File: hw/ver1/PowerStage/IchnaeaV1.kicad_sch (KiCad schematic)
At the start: 11 parts, among them J2 Conn_02x12_Odd_Even, J3 Screw_Terminal_01x09, J4 Screw_Terminal_01x09, J5 Screw_Terminal_01x09, J6 Screw_Terminal_01x09, J8 FanConnector

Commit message: More power plane work. Double mosfets.
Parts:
- added HS1: Heatsink, symbol Mechanical:Heatsink
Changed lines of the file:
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@@
+	)
+	(symbol
+		(lib_id "Mechanical:Heatsink")
+		(at 157.48 44.45 0)
+		(unit 1)
+		(exclude_from_sim no)
+		(in_bom yes)
+		(on_board yes)
+		(dnp no)
+		(fields_autoplaced yes)
+		(property "Reference" "HS1"
+			(at 161.29 41.2749 0)
+			(effects
+				(font
+					(size 1.27 1.27)
+				)
+				(justify left)
+			)
+		)
+		(property "Value" "Heatsink"
+			(at 161.29 43.8149 0)
+			(effects
+				(font
+					(size 1.27 1.27)
+				)
+				(justify left)
+			)
+		)
+		(property "Footprint" ""
+			(at 157.7848 44.45 0)
+			(effects
+				(font
+					(size 1.27 1.27)
+				)
+				(hide yes)
+			)
+		)
+		(property "Datasheet" "~"
+			(at 157.7848 44.45 0)
+			(effects
+				(font
+					(size 1.27 1.27)
+				)
+				(hide yes)
+			)
+		)
+		(property "Description" "Heatsink"
+			(at 157.48 44.45 0)
+			(effects
+				(font
+					(size 1.27 1.27)
+				)
+				(hide yes)
+			)
+		)
+		(instances
+			(project "IchnaeaV1"
+				(path "/1a8ad36a-4b76-4949-97c2-661f12a0b1d9"
+					(reference "HS1")
+					(unit 1)
+				)
+			)
+		)
 	)
 	(symbol

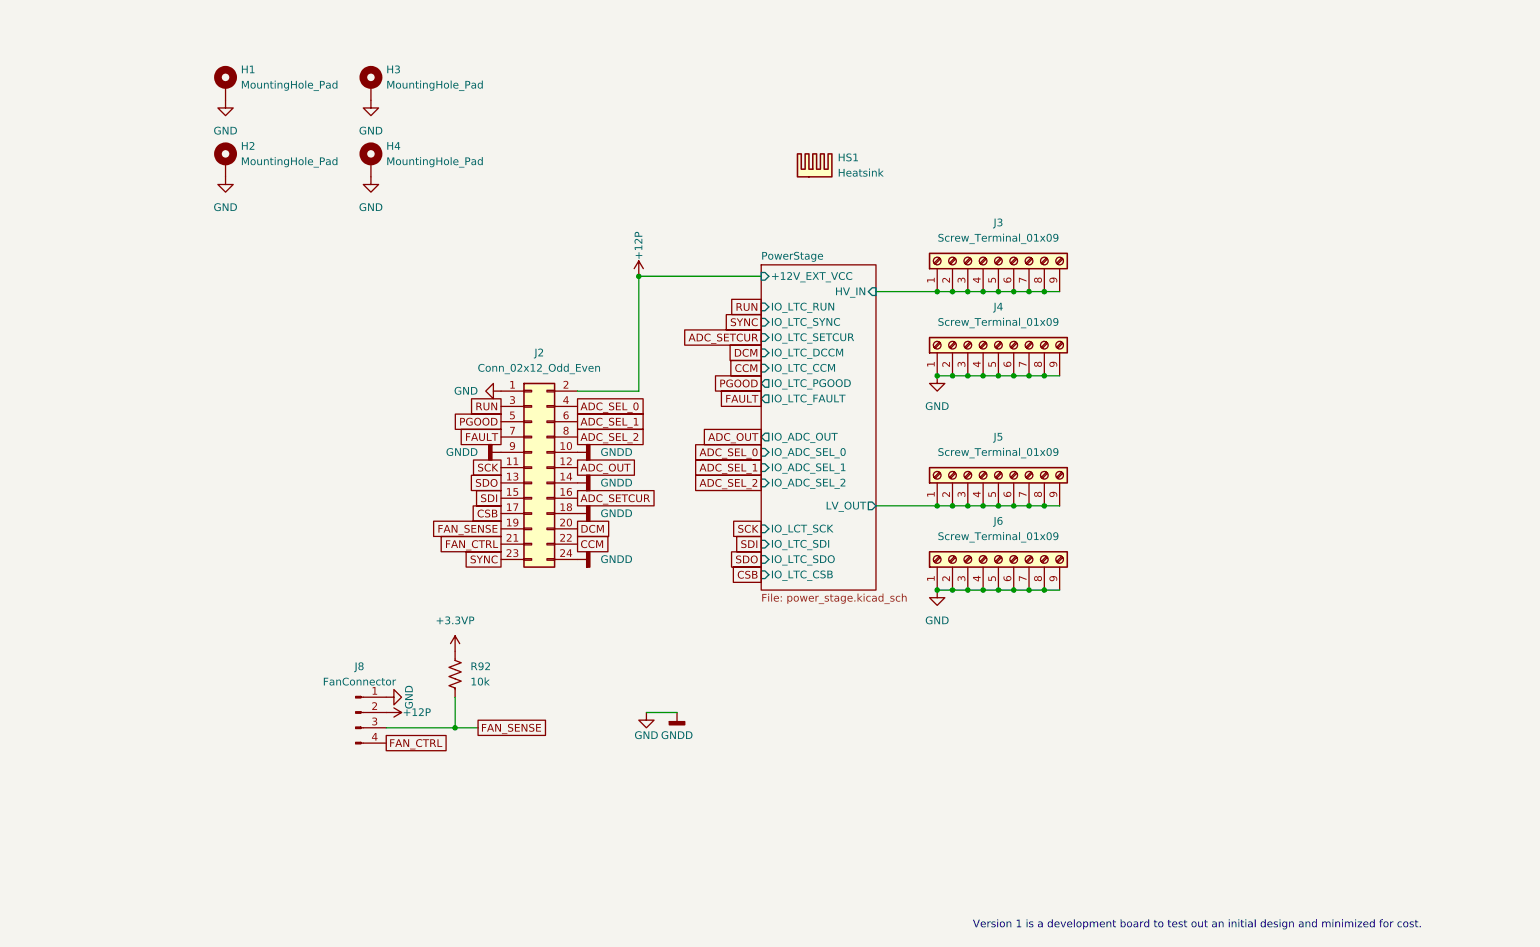
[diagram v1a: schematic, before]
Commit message: Improve power layout. Finish most of the initial routing for the LTC7871
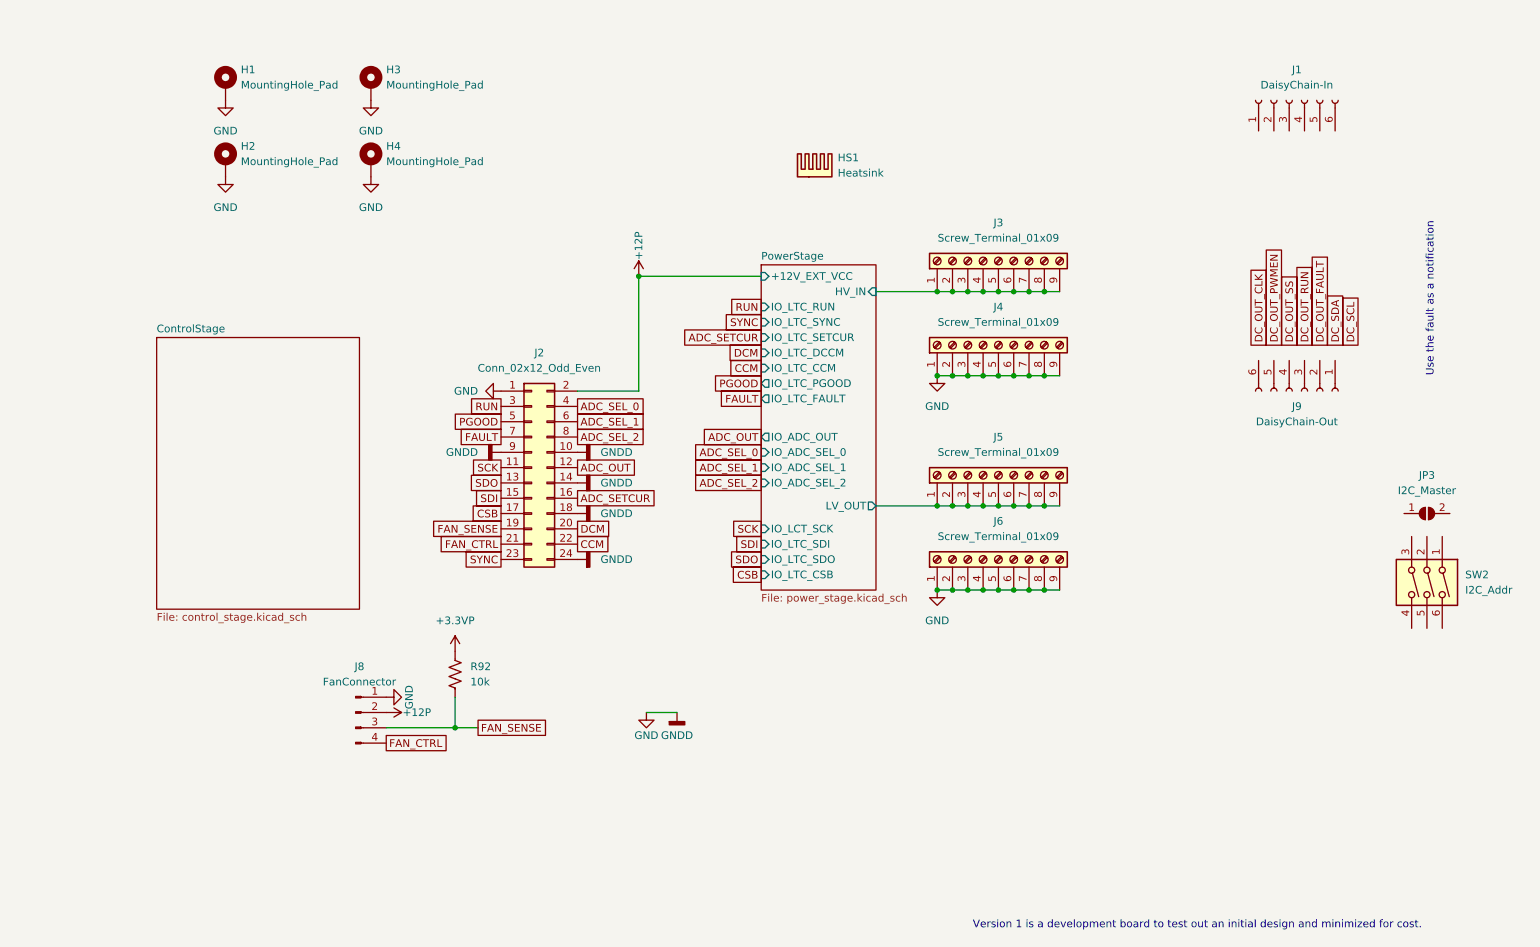
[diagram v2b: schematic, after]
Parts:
- added J1: DaisyChain-In, symbol Connector:Conn_01x06_Socket
- added J9: DaisyChain-Out, symbol Connector:Conn_01x06_Socket
- added JP3: I2C_Master, symbol Jumper:SolderJumper_2_Open
- added SW2: I2C_Addr, Button_Switch_SMD:SW_DIP_SPSTx03_Slide_6.7x9.18mm_W6.73mm_P2.54mm_LowProfile_JPin, symbol Switch:SW_DIP_x03
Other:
- added sheet ControlStage (control_stage.kicad_sch)
- note added: "Use the fault as a notification"

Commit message: Sync morning work to laptop
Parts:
- removed J2: Conn_02x12_Odd_Even, Connector_PinSocket_2.54mm:PinSocket_2x12_P2.54mm_Vertical, symbol Connector_Generic:Conn_02x12_Odd_Even
- removed J8: FanConnector, Connector_Molex:Molex_KK-254_AE-6410-04A_1x04_P2.54mm_Vertical, symbol Connector:Conn_01x04_Pin
- removed JP3: I2C_Master, symbol Jumper:SolderJumper_2_Open
- removed R92: 10k, Resistor_SMD:R_0603_1608Metric, symbol Device:R_US
- removed SW2: I2C_Addr, Button_Switch_SMD:SW_DIP_SPSTx03_Slide_6.7x9.18mm_W6.73mm_P2.54mm_LowProfile_JPin, symbol Switch:SW_DIP_x03
- J1, J9: footprint (none) -> Connector_PinHeader_1.27mm:PinHeader_2x05_P1.27mm_Vertical_SMD; symbol Connector:Conn_01x06_Socket -> Connector:Conn_01x10_Pin
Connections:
- net GND: now also J1.2 (Pin_2), J1.9 (Pin_9), J9.1 (Pin_1), J9.10 (Pin_10)
- net PowerStage/DC_OUT_SDA: now reaches J9.2 (Pin_2)
- net PowerStage/DC_OUT_SS: now reaches J9.3 (Pin_3)
- net PowerStage/DC_OUT_SCL: now reaches J9.4 (Pin_4)
- net PowerStage/DC_OUT_PWMEN: now reaches J9.5 (Pin_5)
- net PowerStage/DC_IN_SYNC: now reaches J1.1 (Pin_1)
- net PowerStage/DC_IN_RUN: now reaches J1.3 (Pin_3)
- net PowerStage/DC_IN_EN: now reaches J1.4 (Pin_4)
- net PowerStage/DC_IN_PWMEN: now reaches J1.5 (Pin_5)
- new net PowerStage/DC_IN_SCL: J1.8 (Pin_8)
- new net PowerStage/DC_IN_SDA: J1.10 (Pin_10)
- new net PowerStage/DC_IN_SS: J1.7 (Pin_7)
- new net PowerStage/DC_OUT_CLK: J9.9 (Pin_9)
- new net PowerStage/DC_OUT_EN: J9.8 (Pin_8)
- new net PowerStage/DC_OUT_RUN: J9.7 (Pin_7)
- no-connect marks 0 -> 2
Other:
- sheet PowerStage ports: added +3V3, +5V, DC_IN_EN, DC_IN_PWMEN, DC_IN_RUN, DC_IN_SCL, DC_IN_SDA, DC_IN_SS, DC_IN_SYNC, DC_OUT_CLK, DC_OUT_EN, DC_OUT_PWMEN, DC_OUT_RUN, DC_OUT_SCL, DC_OUT_SDA, DC_OUT_SS, IO_I2C_SCL, IO_I2C_SDA, IO_LTC_SCK, IO_LTC_SLAVE; removed +12V_EXT_VCC, IO_LCT_SCK
- note added: "RUN pin is 5V drive as Master and logic sense for Slave"
- note removed: "Use the fault as a notification"
- moved on the sheet: HS1, J3, J4, J5, J6

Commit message: Add low voltage switching supply
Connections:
- net PowerStage/LV_OUT renamed LowVoltageSupply/VIN_LV
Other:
- added sheet LowVoltageSupply (low_voltage_supply.kicad_sch)
- sheet PowerStage ports: added none; removed +5V
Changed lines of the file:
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@@
 	)
 	(junction
+		(at 182.88 99.06)
+		(diameter 0)
+		(color 0 0 0 0)
+	)
+	(junction
 		(at 191.77 63.5)
 		(diameter 0)
@@
 	(wire
 		(pts
+			(xy 182.88 134.62) (xy 182.88 99.06)
+		)
+		(stroke
+			(width 0)
+			(type default)
+		)
+	)
+	(wire
+		(pts
 			(xy 194.31 77.47) (xy 196.85 77.47)
 		)
@@
 	(wire
 		(pts
+			(xy 180.34 134.62) (xy 182.88 134.62)
+		)
+		(stroke
+			(width 0)
+			(type default)
+		)
+	)
+	(wire
+		(pts
 			(xy 180.34 63.5) (xy 186.69 63.5)
 		)
@@
 	(wire
 		(pts
-			(xy 180.34 99.06) (xy 186.69 99.06)
+			(xy 182.88 99.06) (xy 186.69 99.06)
+		)
+		(stroke
+			(width 0)
+			(type default)
+		)
+	)
+	(wire
+		(pts
+			(xy 180.34 99.06) (xy 182.88 99.06)
 		)
 		(stroke
@@
 			)
 		)
-		(pin "+5V" output
-			(at 148.59 58.42 180)
-			(effects
-				(font
-					(size 1.27 1.27)
-				)
-				(justify left)
-			)
-		)
 		(pin "+3V3" input
-			(at 148.59 55.88 180)
+			(at 148.59 54.61 180)
 			(effects
 				(font
@@
 				)
 			)
+		)
+	)
+	(sheet
+		(at 148.59 128.27)
+		(size 31.75 12.065)
+		(fields_autoplaced yes)
+		(stroke
+			(width 0.1524)
+			(type solid)
+		)
+		(fill
+			(color 0 0 0 0.0000)
+		)
+		(property "Sheetname" "LowVoltageSupply"
+			(at 148.59 127.5584 0)
+			(effects
+				(font
+					(size 1.27 1.27)
+				)
+				(justify left bottom)
+			)
+		)
+		(property "Sheetfile" "low_voltage_supply.kicad_sch"
+			(at 148.59 140.9196 0)
+			(effects
+				(font
+					(size 1.27 1.27)
+				)
+				(justify left top)
+			)
+		)
+		(pin "VIN_LV" input
+			(at 180.34 134.62 0)
+			(effects
+				(font
+					(size 1.27 1.27)
+				)
+				(justify right)
+			)
+		)
+		(pin "VOUT_LV" output
+			(at 148.59 134.62 180)
+			(effects
+				(font
+					(size 1.27 1.27)
+				)
+				(justify left)
+			)
+		)
+		(instances
+			(project "IchnaeaV1"
+				(path "/1a8ad36a-4b76-4949-97c2-661f12a0b1d9"
+					(page "10")
+				)
+			)

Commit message: Sync tonight's effort
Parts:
- H1, H2, H3, H4: Digikey (none) -> N/A; LCSC (none) -> N/A
- HS1: Digikey (none) -> ATS-CPX070070010-209-C1-R0; LCSC (none) -> N/A
- J1, J9: Digikey (none) -> 1175-1629-ND; LCSC (none) -> N/A
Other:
- sheet ControlStage ports: added CTL_IN_ADC, CTL_IN_FAULT, CTL_IN_PGOOD, CTL_IN_SDI, CTL_IN_SLAVE, CTL_IO_SDA, CTL_OUT_ADC_SEL_0, CTL_OUT_ADC_SEL_1, CTL_OUT_ADC_SEL_2, CTL_OUT_CCM, CTL_OUT_CSB, CTL_OUT_DCM, CTL_OUT_RUN, CTL_OUT_SCK, CTL_OUT_SCL, CTL_OUT_SDO, CTL_OUT_SETCUR, CTL_OUT_SYNC, PWR_OUT_3V3, VSupply; removed none
- note removed: "RUN pin is 5V drive as Master and logic sense for Slave"
- moved on the sheet: H1, H2, H3, H4, HS1

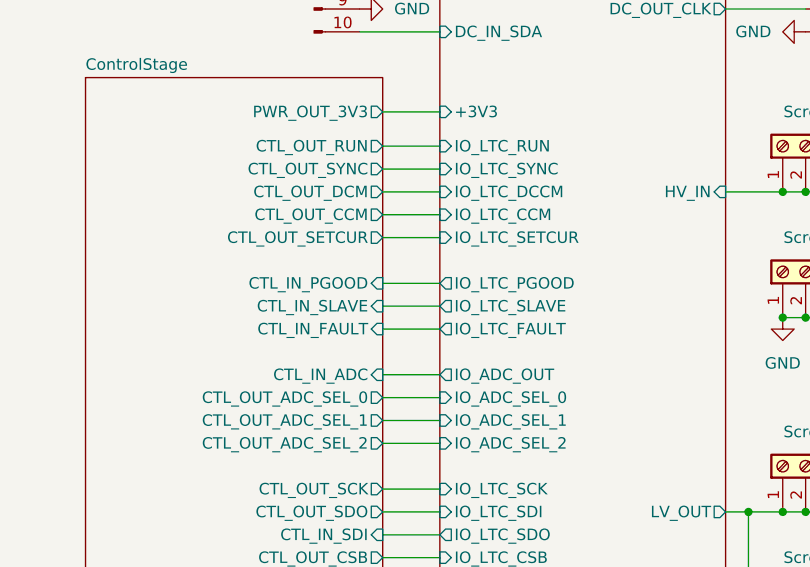
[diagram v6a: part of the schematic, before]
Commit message: Start optimizing some of the layout to make room for control circuitry
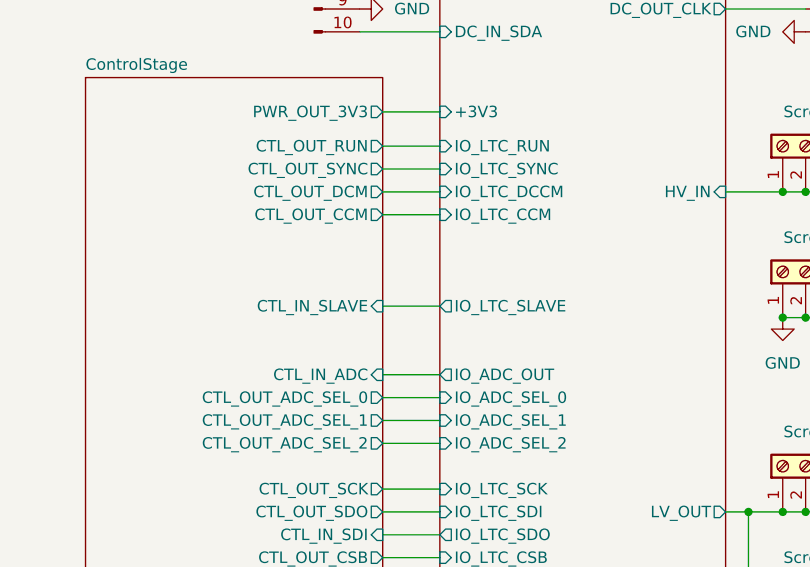
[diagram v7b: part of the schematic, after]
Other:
- sheet ControlStage ports: added none; removed CTL_IN_FAULT, CTL_IN_PGOOD, CTL_OUT_SETCUR
- sheet PowerStage ports: added none; removed IO_LTC_FAULT, IO_LTC_PGOOD, IO_LTC_SETCUR
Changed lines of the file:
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@@
-	(wire
-		(pts
-			(xy 142.24 68.58) (xy 148.59 68.58)
-		)
-		(stroke
-			(width 0)
-			(type default)
-		)
-	)
 	(wire
 		(pts
@@
 	(wire
 		(pts
-			(xy 142.24 78.74) (xy 148.59 78.74)
-		)
-		(stroke
-			(width 0)
-			(type default)
-		)
-	)
-	(wire
-		(pts
 			(xy 180.34 99.06) (xy 182.88 99.06)
 		)
@@
 		(pts
 			(xy 180.34 40.64) (xy 189.23 40.64)
-		)
-		(stroke
-			(width 0)
-			(type default)
-		)
-	)
-	(wire
-		(pts
-			(xy 142.24 73.66) (xy 148.59 73.66)
 		)
 		(stroke
@@
 			)
 		)
-		(pin "IO_LTC_PGOOD" output
-			(at 148.59 73.66 180)
-			(effects
-				(font
-					(size 1.27 1.27)
-				)
-				(justify left)
-			)
-		)
 		(pin "IO_LTC_SDI" input
 			(at 148.59 99.06 180)
@@
 			)
 		)
-		(pin "IO_LTC_FAULT" output
-			(at 148.59 78.74 180)
-			(effects
-				(font
-					(size 1.27 1.27)
-				)
-				(justify left)
-			)
-		)
 		(pin "IO_LTC_CSB" input
 			(at 148.59 104.14 180)
@@
 		(pin "IO_LTC_SYNC" input
 			(at 148.59 60.96 180)
-			(effects
-				(font
-					(size 1.27 1.27)
-				)
-				(justify left)
-			)
-		)
-		(pin "IO_LTC_SETCUR" input
-			(at 148.59 68.58 180)
 			(effects
 				(font
@@
 			)
 		)
-		(pin "CTL_IN_FAULT" input
-			(at 142.24 78.74 0)
-			(effects
-				(font
-					(size 1.27 1.27)
-				)
-				(justify right)
-			)
-		)
 		(pin "CTL_IN_ADC" input
 			(at 142.24 83.82 0)
@@
 			)
 		)
-		(pin "CTL_IN_PGOOD" input
-			(at 142.24 73.66 0)
-			(effects
-				(font
-					(size 1.27 1.27)
-				)
-				(justify right)
-			)
-		)
 		(pin "CTL_IN_SLAVE" input
 			(at 142.24 76.2 0)
@@
 			(effects
 				(font
-					(size 1.27 1.27)
-				)
-				(justify right)
-			)
-		)
-		(pin "CTL_OUT_SETCUR" output
-			(at 142.24 68.58 0)
-			(effects
-				(font
